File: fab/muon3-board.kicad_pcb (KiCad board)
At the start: 4 copper layers, 160 x 120 mm, 241 parts

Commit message: board: ratsnest topology analysis + placement optimization (-24% weighted)
Add tools/ratsnest.py: builds the ratsnest (per-net MST), weights nets by a
datasheet/DESIGN_RULES routing priority (RF 10 > AFE hi-Z 8 > ... > power 1
> GND 0), and reports weighted airwire length + zone crossings.

Verdict: macro-topology is sound — ZERO w>=4 nets cross a zone (RF/AFE/HV/
high-speed digital all stay local; only power/GND span the board).

Optimizations (weighted airwire 6642 -> 5078, -24%):
- AFE bias/thresholds made per-channel (VBOTF, V*_DAC) instead of board-
  spanning shared nets: kills the 98/69 mm nets AND fixes the freeze
  requirement for independent per-channel thresholds.
- Dropped the analog AOUT tap from the FPGA header: AOUT 37.5 -> 23.5 mm.
- U.FL moved directly below the nRF ANT pad: RF_ANT 25 -> ~8 mm.
- Clamp diodes pulled tight to the TIA input: shorter INA summing node.

LAYOUT.md: topology section with the weight->layer table and verdict.
DRC-clean, zero overlaps.

Co-Authored-By: Claude Opus 4.8 <noreply@anthropic.com>
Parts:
- moved J_ANT 30.5 mm to (36.0, 83.0)
- moved D_CLH0 2.50 mm to (65.5, 54.5)
- moved D_CLH1 2.50 mm to (88.5, 54.5)
- moved D_CLH2 2.50 mm to (111.5, 54.5)
- moved D_CLH3 2.50 mm to (134.5, 54.5)
- moved D_CLL0 2.50 mm to (74.5, 54.5)
- moved D_CLL1 2.50 mm to (97.5, 54.5)
- moved D_CLL2 2.50 mm to (120.5, 54.5)
- moved D_CLL3 2.50 mm to (143.5, 54.5)
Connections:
- C_VB0 pad 1: VBOTF -> VBOTF0
- C_VB1 pad 1: VBOTF -> VBOTF1
- C_VB2 pad 1: VBOTF -> VBOTF2
- C_VB3 pad 1: VBOTF -> VBOTF3
- J_FPGA0 pad 3: AOUT0 -> GND
- J_FPGA1 pad 3: AOUT1 -> GND
- J_FPGA2 pad 3: AOUT2 -> GND
- J_FPGA3 pad 3: AOUT3 -> GND
- R_THH0 pad 1: VTHH_DAC -> VTHH_DAC0
- R_THH1 pad 1: VTHH_DAC -> VTHH_DAC1
- R_THH2 pad 1: VTHH_DAC -> VTHH_DAC2
- R_THH3 pad 1: VTHH_DAC -> VTHH_DAC3
- R_THL0 pad 1: VTHL_DAC -> VTHL_DAC0
- R_THL1 pad 1: VTHL_DAC -> VTHL_DAC1
- R_THL2 pad 1: VTHL_DAC -> VTHL_DAC2
- R_THL3 pad 1: VTHL_DAC -> VTHL_DAC3
- R_VB0 pad 1: VBOT_DAC -> VBOT_DAC0
- R_VB0 pad 2: VBOTF -> VBOTF0
- R_VB1 pad 1: VBOT_DAC -> VBOT_DAC1
- R_VB1 pad 2: VBOTF -> VBOTF1
- R_VB2 pad 1: VBOT_DAC -> VBOT_DAC2
- R_VB2 pad 2: VBOTF -> VBOTF2
- R_VB3 pad 1: VBOT_DAC -> VBOT_DAC3
- R_VB3 pad 2: VBOTF -> VBOTF3
- U_TIA0 pad 4: VBOTF -> VBOTF0
- U_TIA1 pad 4: VBOTF -> VBOTF1
- U_TIA2 pad 4: VBOTF -> VBOTF2
- U_TIA3 pad 4: VBOTF -> VBOTF3

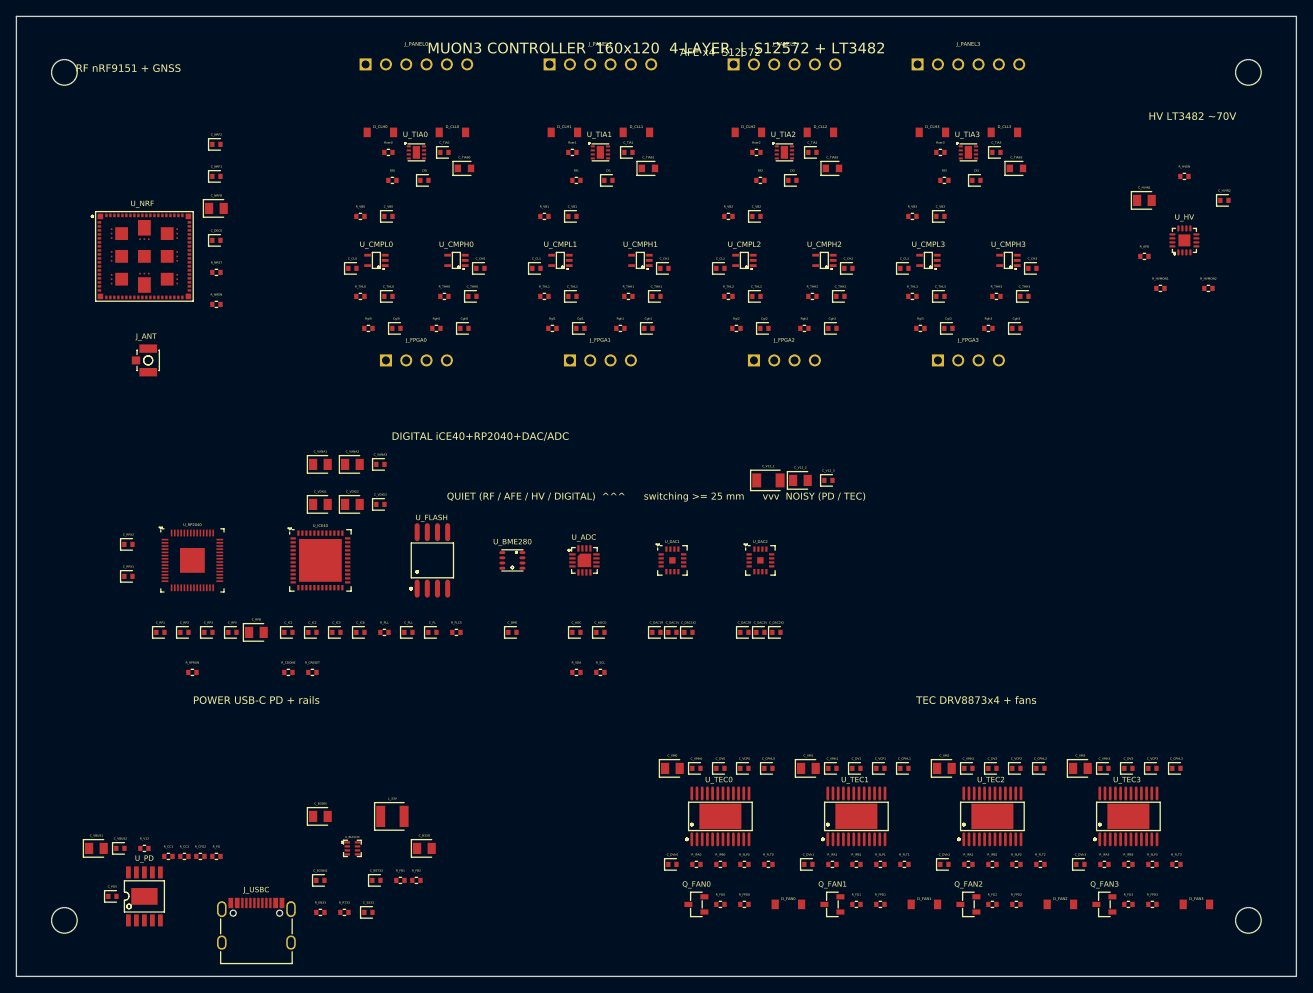
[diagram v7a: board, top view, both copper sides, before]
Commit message: board: debug bay + test points + inter-IC bus connectivity (265 comp, DRC-clean)
Debuggability / connectivity pass.

Debug bay (board/debug.tsx) in the free pocket between DIGITAL and HV:
- 14 labelled test points: all rails (VANA/VDIG/V12/VCORE/V1V2/GND) +
  SPI/I2C buses + GNSS PPS + the *divided* HV monitor (never raw 70 V).
- per-channel TP_AO analog probe on each AFE TIA output (in afe.tsx,
  next to the channel to avoid a long summing-node stub).
- SWD headers (RP2040 + nRF9151), iCE40 SPI-config header (J_CFG),
  stdio-UART header; vertical/doubleRow so they column cleanly.
- RUN + BOOTSEL buttons; power-good + heartbeat status LEDs.

Connectivity closed (were single-pad stubs):
- RP2040 <-> flash QSPI boot bus.
- RP2040 <-> DAC SPI + I2C to BME280/ADS7128.
- RP2040 <-> iCE40 config (SPI slave-load) + CDONE/CRESET monitor.
- 8 AFE comparator outputs -> iCE40 counters.
- nRF9151 GNSS 1 PPS -> iCE40 timestamp; nRF/RP2040 SWD to headers.
- RP2040 USB shared onto the USB-C data pair (flashable in place).

Panel connector 6 -> 10-pin double-row hybrid (decision 6): one locking
connector per tile now carries SiPM signal+shield, HV bias, both NTCs, the
DRV8873 H-bridge outputs, and the 12 V fan feed + return (OA/OB/FANN shared
by index with tec.tsx).

Docs: README status table + LAYOUT.md debug/connectivity section (incl. the
note that weighted airwire rose because real buses got connected, not a
placement regression). ratsnest.py gains the DEBUG zone. fab/ regenerated.

Co-Authored-By: Claude Opus 4.8 <noreply@anthropic.com>
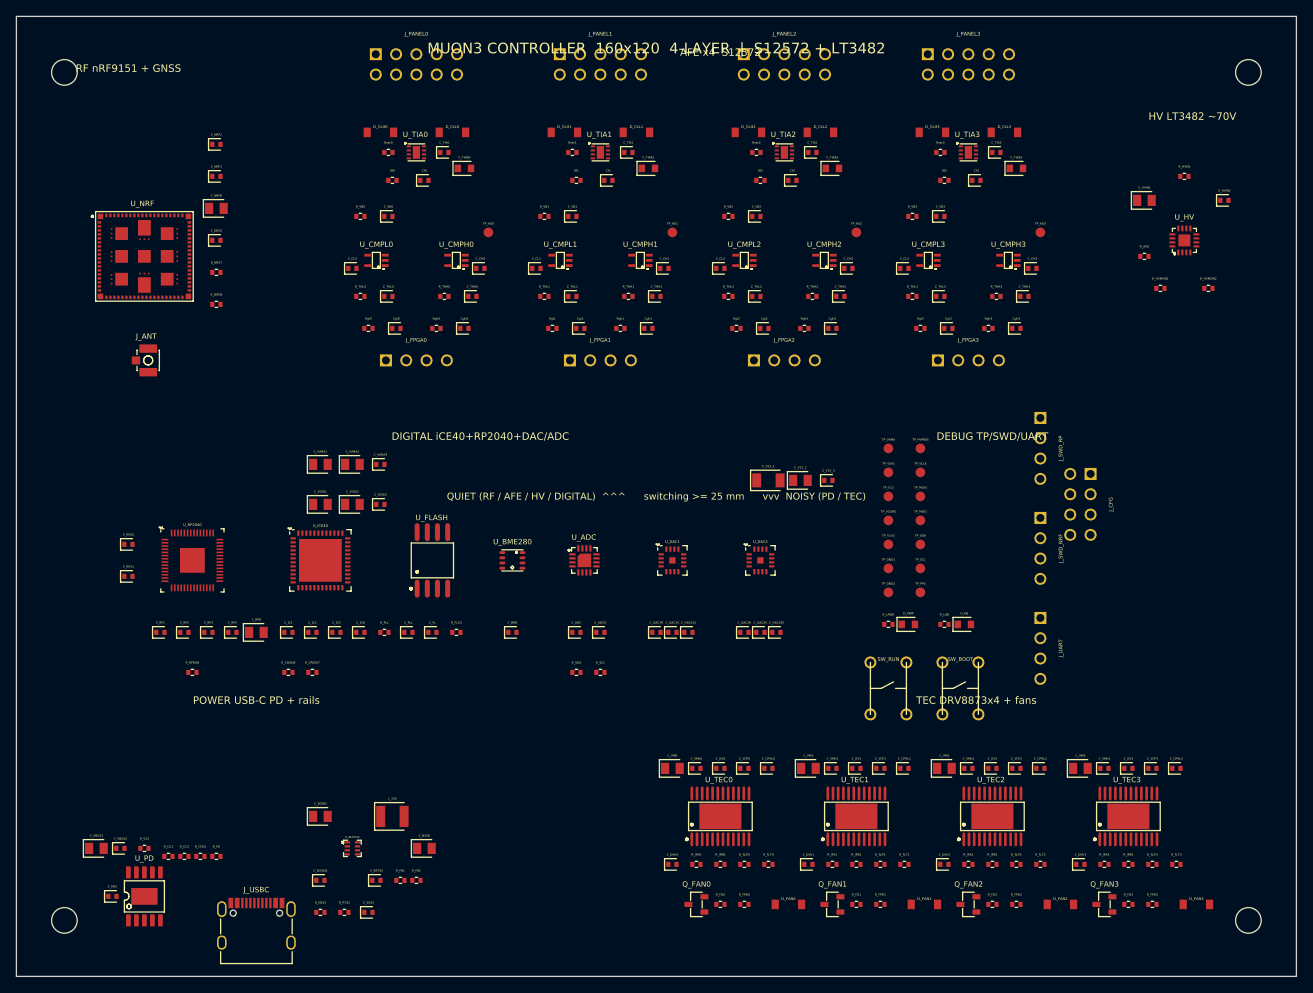
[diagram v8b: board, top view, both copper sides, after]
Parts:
- added D_HB: LED, tscircuit:led_0603, F.Cu at (138.5, 116.0)
- added D_PWR: LED, tscircuit:led_0603, F.Cu at (131.5, 116.0)
- added J_CFG: J_CFG, tscircuit:pin_header_pinrow8_nopinlabels_rows2, F.Cu at (153.0, 101.0)
- added J_SWD_NRF: J_SWD_NRF, tscircuit:pin_header_pinrow4_nopinlabels, F.Cu at (148.0, 106.5)
- added J_SWD_RP: J_SWD_RP, tscircuit:pin_header_pinrow4_nopinlabels, F.Cu at (148.0, 94.0)
- added J_UART: J_UART, tscircuit:pin_header_pinrow4_nopinlabels, F.Cu at (148.0, 119.0)
- added R_LHB: 330Ω, tscircuit:resistor_res0402, F.Cu at (136.0, 116.0)
- added R_LPWR: 1kΩ, tscircuit:resistor_res0402, F.Cu at (129.0, 116.0)
- added SW_BOOT: SW_BOOT, tscircuit:push_button_pushbutton, F.Cu at (138.0, 124.0)
- added SW_RUN: SW_RUN, tscircuit:push_button_pushbutton, F.Cu at (129.0, 124.0)
- added TP_AO0: TP_AO0, tscircuit:test_point_smtpad_circle_d1.2, F.Cu at (79.0, 67.0)
- added TP_AO1: TP_AO1, tscircuit:test_point_smtpad_circle_d1.2, F.Cu at (102.0, 67.0)
- added TP_AO2: TP_AO2, tscircuit:test_point_smtpad_circle_d1.2, F.Cu at (125.0, 67.0)
- added TP_AO3: TP_AO3, tscircuit:test_point_smtpad_circle_d1.2, F.Cu at (148.0, 67.0)
- added TP_GND1: TP_GND1, tscircuit:test_point_smtpad_circle_d1.2, F.Cu at (129.0, 109.0)
- added TP_GND2: TP_GND2, tscircuit:test_point_smtpad_circle_d1.2, F.Cu at (129.0, 112.0)
- added TP_HVMON: TP_HVMON, tscircuit:test_point_smtpad_circle_d1.2, F.Cu at (133.0, 94.0)
- added TP_MISO: TP_MISO, tscircuit:test_point_smtpad_circle_d1.2, F.Cu at (133.0, 103.0)
- added TP_MOSI: TP_MOSI, tscircuit:test_point_smtpad_circle_d1.2, F.Cu at (133.0, 100.0)
- added TP_PPS: TP_PPS, tscircuit:test_point_smtpad_circle_d1.2, F.Cu at (133.0, 112.0)
- added TP_SCL: TP_SCL, tscircuit:test_point_smtpad_circle_d1.2, F.Cu at (133.0, 109.0)
- added TP_SCLK: TP_SCLK, tscircuit:test_point_smtpad_circle_d1.2, F.Cu at (133.0, 97.0)
- added TP_SDA: TP_SDA, tscircuit:test_point_smtpad_circle_d1.2, F.Cu at (133.0, 106.0)
- added TP_V12: TP_V12, tscircuit:test_point_smtpad_circle_d1.2, F.Cu at (129.0, 100.0)
- added TP_V1V2: TP_V1V2, tscircuit:test_point_smtpad_circle_d1.2, F.Cu at (129.0, 106.0)
- added TP_VANA: TP_VANA, tscircuit:test_point_smtpad_circle_d1.2, F.Cu at (129.0, 94.0)
- added TP_VCORE: TP_VCORE, tscircuit:test_point_smtpad_circle_d1.2, F.Cu at (129.0, 103.0)
- added TP_VDIG: TP_VDIG, tscircuit:test_point_smtpad_circle_d1.2, F.Cu at (129.0, 97.0)
- J_PANEL0, J_PANEL1, J_PANEL2, J_PANEL3: footprint tscircuit:pin_header_pinrow6_nopinlabels_female -> tscircuit:pin_header_pinrow10_nopinlabels_female_rows2
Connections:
- J_PANEL0 pad 2: HV0 -> GND
- J_PANEL0 pad 3: GND -> HV0
- J_PANEL0 pad 4: NTC_C0 -> GND
- J_PANEL0 pad 5: NTC_H0 -> NTC_C0
- J_PANEL0 pad 6: GND -> NTC_H0
- J_PANEL1 pad 2: HV1 -> GND
- J_PANEL1 pad 3: GND -> HV1
- J_PANEL1 pad 4: NTC_C1 -> GND
- J_PANEL1 pad 5: NTC_H1 -> NTC_C1
- J_PANEL1 pad 6: GND -> NTC_H1
- J_PANEL2 pad 2: HV2 -> GND
- J_PANEL2 pad 3: GND -> HV2
- J_PANEL2 pad 4: NTC_C2 -> GND
- J_PANEL2 pad 5: NTC_H2 -> NTC_C2
- J_PANEL2 pad 6: GND -> NTC_H2
- J_PANEL3 pad 2: HV3 -> GND
- J_PANEL3 pad 3: GND -> HV3
- J_PANEL3 pad 4: NTC_C3 -> GND
- J_PANEL3 pad 5: NTC_H3 -> NTC_C3
- J_PANEL3 pad 6: GND -> NTC_H3
- U_ADC pad 13: (no net) -> I2C_SCL
- U_ADC pad 14: (no net) -> I2C_SDA
- U_BME280 pad 3: (no net) -> I2C_SDA
- U_BME280 pad 4: (no net) -> I2C_SCL
- U_BME280 pad 5: (no net) -> GND
- U_FLASH pad 2: (no net) -> QSPI_SD1
- U_FLASH pad 3: (no net) -> QSPI_SD2
- U_FLASH pad 5: (no net) -> QSPI_SD0
- U_FLASH pad 6: (no net) -> QSPI_SCLK
- U_FLASH pad 7: (no net) -> QSPI_SD3
- U_ICE40 pad 14: (no net) -> ICE_SO
- U_ICE40 pad 15: (no net) -> ICE_SCK
- U_ICE40 pad 16: (no net) -> ICE_SS
- U_ICE40 pad 17: (no net) -> ICE_SI
- U_ICE40 pad 2: (no net) -> FPAL2
- U_ICE40 pad 3: (no net) -> FPAL3
- U_ICE40 pad 4: (no net) -> FPAH2
- U_ICE40 pad 45: (no net) -> FPAH1
- U_ICE40 pad 46: (no net) -> FPAL0
- U_ICE40 pad 47: (no net) -> FPAH0
- U_ICE40 pad 48: (no net) -> FPAL1
- U_ICE40 pad 6: (no net) -> FPAH3
- U_ICE40 pad 9: (no net) -> PPS
- U_NRF pad 21: (no net) -> PPS
- U_NRF pad 3: (no net) -> NRF_SWDCLK
- U_NRF pad 4: (no net) -> NRF_SWDIO
- U_RP2040 pad 13: (no net) -> ICE_SCK
- U_RP2040 pad 14: (no net) -> ICE_SI
- U_RP2040 pad 15: (no net) -> ICE_SO
- U_RP2040 pad 16: (no net) -> ICE_SS
- U_RP2040 pad 17: (no net) -> ICE_CRESET
- U_RP2040 pad 18: (no net) -> ICE_CDONE
- U_RP2040 pad 2: (no net) -> UART_TX
- U_RP2040 pad 24: (no net) -> RP_SWCLK
- U_RP2040 pad 25: (no net) -> RP_SWD
- U_RP2040 pad 27: (no net) -> SPI_MISO
- U_RP2040 pad 28: (no net) -> DAC1_CS
- U_RP2040 pad 29: (no net) -> SPI_SCLK
- U_RP2040 pad 3: (no net) -> UART_RX
- U_RP2040 pad 30: (no net) -> SPI_MOSI
- U_RP2040 pad 31: (no net) -> DAC2_CS
- U_RP2040 pad 37: (no net) -> RP_LED
- U_RP2040 pad 46: (no net) -> USB_DM
- U_RP2040 pad 47: (no net) -> USB_DP
- U_RP2040 pad 51: (no net) -> QSPI_SD3
- U_RP2040 pad 52: (no net) -> QSPI_SCLK
- U_RP2040 pad 53: (no net) -> QSPI_SD0
- U_RP2040 pad 54: (no net) -> QSPI_SD2
- U_RP2040 pad 55: (no net) -> QSPI_SD1
- U_RP2040 pad 56: (no net) -> FLASH_CS
- U_RP2040 pad 6: (no net) -> I2C_SDA
- U_RP2040 pad 7: (no net) -> I2C_SCL
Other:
- board text added: "DEBUG TP/SWD/UART"
- board text added: "test points + programming headers + buttons/LEDs"
